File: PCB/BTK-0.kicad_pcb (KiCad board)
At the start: 4 copper layers, 167.1 x 105 mm, 110 parts, among them J1 USB_C_Receptacle_USB2.0_16P, J2 Battery, J3 Conn_01x16_Pin, J4 Conn_01x16_Socket, SW1 EN, SW10 1,2, SW11 2,2, SW12 3,2, SW13 4,2, SW14 5,2, SW15 6,2, SW16 1,3, SW17 2,3, SW18 3,3, SW19 4,3, SW2 BOOT, SW20 5,3, SW21 6,3, SW22 1,4, SW23 2,4, SW24 3,4, SW25 4,4, SW26 5,4, SW27 6,4, SW28 1,4, SW29 2,4, SW3 RotaryEncoder_Switch_MP, SW30 3,4, SW31 4,4, SW32 5,4, SW33 6,4, SW4 1,1, SW5 2,1, SW6 3,1, SW7 4,1, SW8 5,1, SW9 6,1, U1 NCP1117-3.3_SOT223, U2 NCP1117-3.3_SOT223, U3 USBLC6-2SC6, U4 ESP32-C6-MINI-1, U5 TVS1400DRV, U6 BQ24075RGT

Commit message: new switches kailh sockets
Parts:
- SW10, SW11, SW12, SW13, SW14, SW15, SW16, SW17, SW18, SW19, SW20, SW21, SW22, SW23, SW24, SW25, SW26, SW27, SW28, SW29, SW30, SW31, SW32, SW33, SW4, SW5, SW6, SW7, SW8, SW9: footprint kb_switch:SW_MX_reversible -> kb_switch:Kailh_socket_MX_reversible
- moved H4 266.2 mm to (131.5, 72.5)
- moved H3 160.4 mm to (135.3, 10.8)
- moved H1 156.3 mm to (37.0, 2.00)
- moved D33 155.2 mm to (133.6, 76.2), turned to 135 degrees
- moved D35 150.3 mm to (133.8, 20.7), turned to 180 degrees
- moved D34 150.2 mm to (133.8, 39.7)
- moved D32 144.9 mm to (113.5, 94.1), turned to 180 degrees
- moved J4 144.5 mm to (138.6, 34.3)
- moved SW10 144.5 mm to (8.84, 27.6), turned to 180 degrees
- moved SW11 144.5 mm to (27.9, 27.6), turned to 180 degrees
- moved SW12 144.5 mm to (46.9, 24.6), turned to 180 degrees
- moved SW13 144.5 mm to (66.0, 22.6), turned to 180 degrees
- moved SW14 144.5 mm to (85.0, 24.6), turned to 180 degrees
- moved SW15 144.5 mm to (104.1, 26.6), turned to 180 degrees
- moved SW16 144.5 mm to (8.84, 46.7), turned to 180 degrees
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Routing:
- net /IO1: track 233.0 -> 295.2 mm, vias 1 -> 6
- net /IO4: track 287.1 -> 339.5 mm, vias 0 -> 5
- net /IO2: track 193.0 -> 245.0 mm, vias 1 -> 6
- net /IO5: track 271.3 -> 322.5 mm, vias 0 -> 5
- net /IO0: track 252.9 -> 302.6 mm, vias 1 -> 6
- net /IO23: track 54.9 -> 16.5 mm
- net /IO18: track 185.2 -> 151.5 mm, vias 3 -> 2
- net /IO15: track 168.4 -> 138.9 mm, vias 1 -> 2
- net /IO7: track 159.2 -> 170.2 mm, vias 1 -> 6
- net Net-(D34-A): track 15.8 -> 5.08 mm, vias 0 -> 1
- net /IO14: track 150.6 -> 140.9 mm, vias 1 -> 2
- net Net-(D35-A): track 14.1 -> 5.08 mm, vias 0 -> 1
- net /IO22: track 41.6 -> 47.7 mm
- net Net-(D33-A): track 11.0 -> 5.08 mm, vias 0 -> 1
- net /IO6: track 149.4 -> 145.2 mm
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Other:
- board size 167.1 x 105 mm -> 162.1 x 105 mm

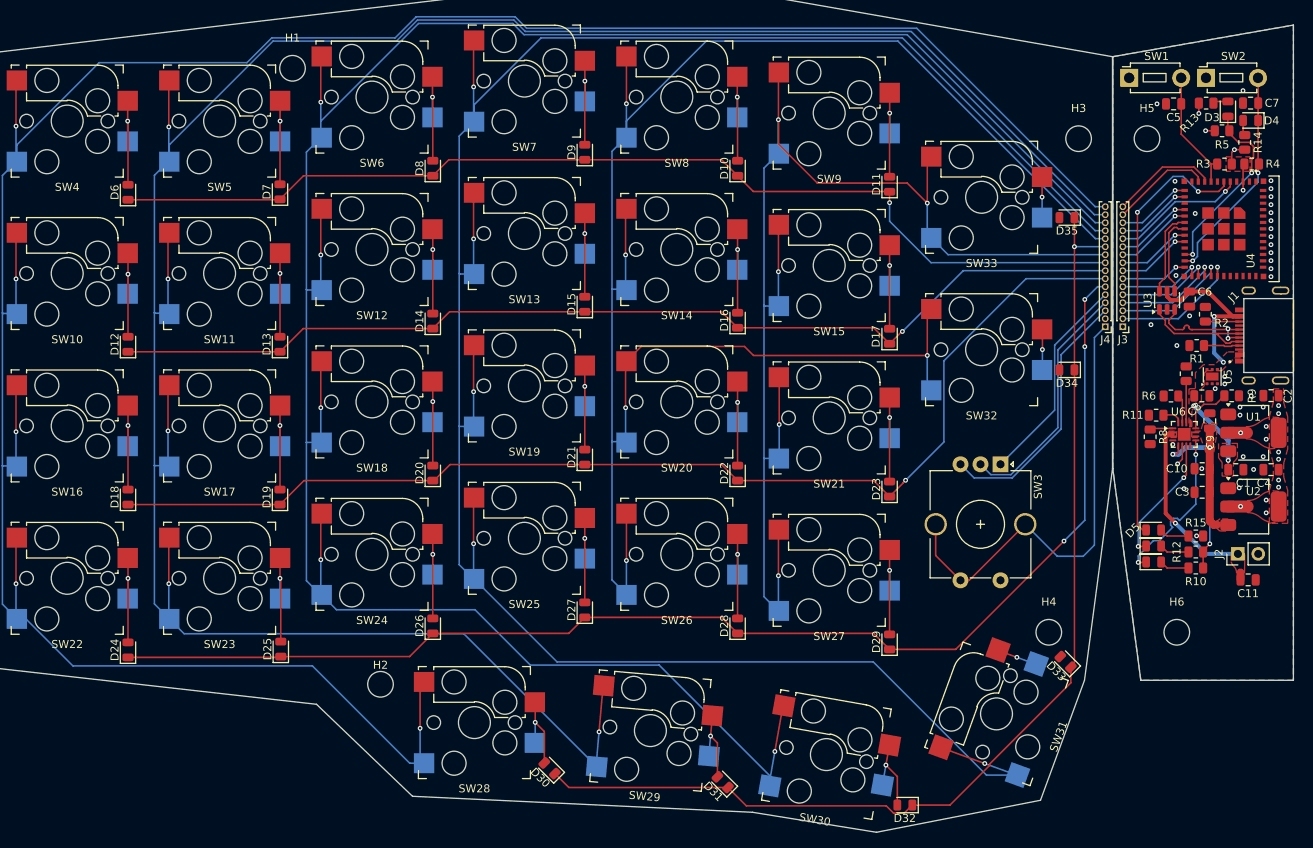
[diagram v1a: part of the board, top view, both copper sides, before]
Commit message: fixed power scheme, on/off switch to power
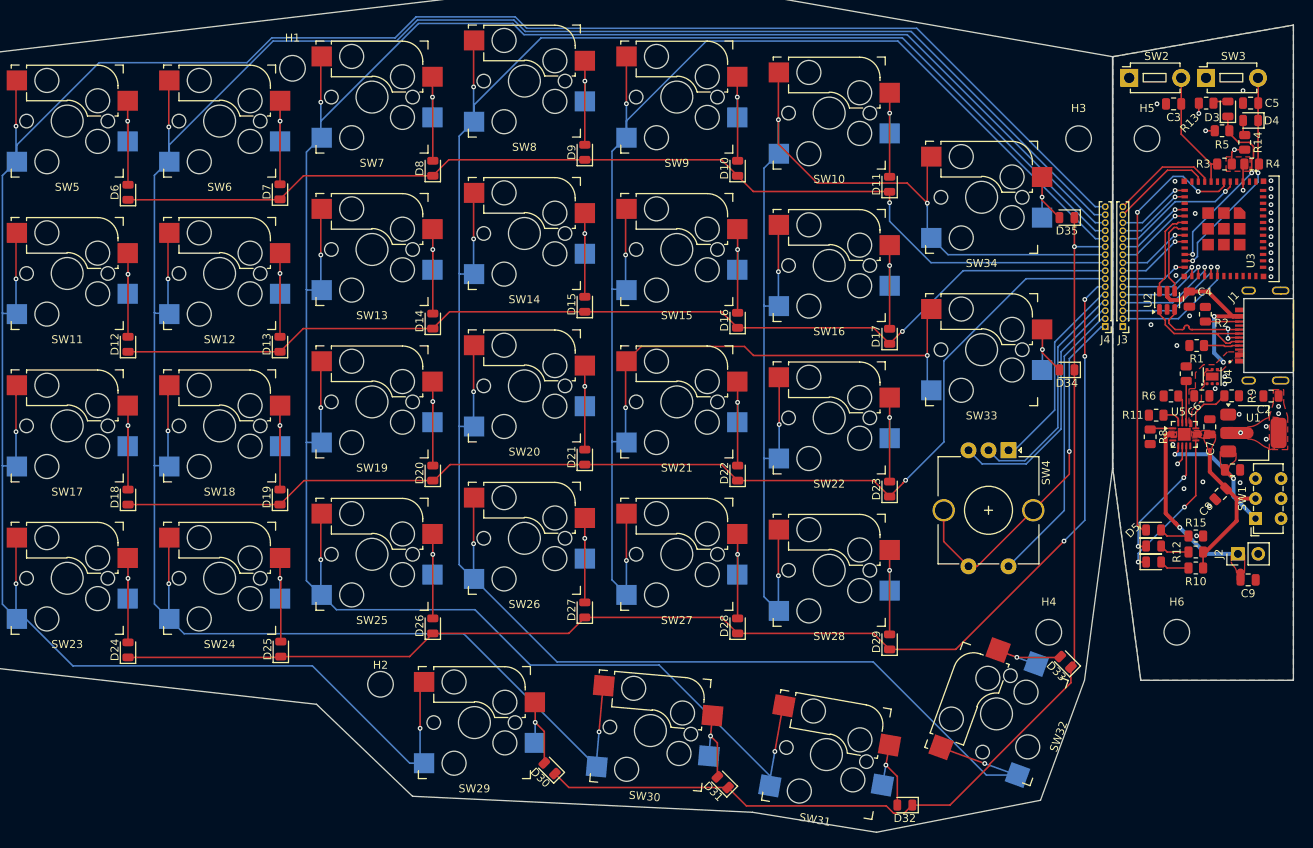
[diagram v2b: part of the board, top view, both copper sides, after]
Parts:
- removed the C1 at (154.9, 52.2)
- removed the C2 at (159.3, 42.9)
- removed the U1 at (157.1, 47.6)
- added SW1: SW_SPDT, Button_Switch_THT:SW_E-Switch_EG1271_SPDT, F.Cu at (157.4, 58.3)
- moved C2 9.20 mm to (159.3, 43.0)
- moved U1 9.20 mm to (157.1, 47.6)
- moved C1 4.71 mm to (154.5, 52.2), turned to 0 degrees
- moved C8 3.91 mm to (153.0, 55.2), turned to -135 degrees
- moved SW4 2.02 mm to (126.5, 49.8)
- moved C7 0.75 mm to (151.7, 46.8)
- renumbered C3 to C1, C4 to C2, C5 to C3, C6 to C4, C7 to C5, C8 to C6, C9 to C7, C10 to C8, C11 to C9, SW9 to SW10, SW10 to SW11, SW11 to SW12, SW12 to SW13, SW13 to SW14, SW14 to SW15, SW15 to SW16, SW16 to SW17, SW17 to SW18, SW18 to SW19, SW1 to SW2, SW19 to SW20, SW20 to SW21, SW21 to SW22, SW22 to SW23, SW23 to SW24, SW24 to SW25, SW25 to SW26, SW26 to SW27, SW27 to SW28, SW28 to SW29, SW2 to SW3, SW29 to SW30, SW30 to SW31, SW31 to SW32, SW32 to SW33, SW33 to SW34, SW3 to SW4, SW4 to SW5, SW5 to SW6, SW6 to SW7, SW7 to SW8, SW8 to SW9, U2 to U1, U3 to U2, U4 to U3, U5 to U4, U6 to U5
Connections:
- C7 pad 1: VCC -> VOUT
- C8 pad 1: VCC -> VOUT
- R10 pad 1: VCC -> VOUT
- R12 pad 2: VCC -> VOUT
- U5 pad 10: VCC -> VOUT
- U5 pad 11: VCC -> VOUT
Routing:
- net /IO23: track 16.5 -> 52.8 mm
- net VOUT: track 0.00 -> 21.7 mm
- net VCC: track 35.8 -> 18.3 mm, vias 3 -> 2
- net GND: track 60.5 -> 48.8 mm, vias 36 -> 32
- net VBUS: track 30.1 -> 21.0 mm, vias 4 -> 2
- net Net-(D33-A): track 5.08 -> 10.6 mm
- net Net-(D35-A): track 5.08 -> 8.54 mm
- net Net-(D34-A): track 5.08 -> 8.50 mm
- net +3V3: track 14.8 -> 12.5 mm, vias 17 -> 10
- net Net-(D2-K): track 20.7 -> 19.2 mm
- net /IO21: track 44.2 -> 42.7 mm
- net /IO22: track 47.7 -> 46.2 mm
- net /IO20: track 38.7 -> 37.2 mm
- added copper zone on F.Cu, net VOUT

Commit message: exported cad
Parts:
- moved D10 141.5 mm to (-48.9, 13.9)
- moved D11 141.5 mm to (-29.9, 15.9)
- moved D12 141.5 mm to (-125.1, 36.0)
- moved D13 141.5 mm to (-106.1, 36.0)
- moved D14 141.5 mm to (-87.0, 33.0)
- moved D15 141.5 mm to (-68.0, 30.9)
- moved D16 141.5 mm to (-48.9, 33.0)
- moved D17 141.5 mm to (-29.9, 35.0)
- moved D18 141.5 mm to (-125.1, 55.0)
- moved D19 141.5 mm to (-106.1, 55.0)
- moved D20 141.5 mm to (-87.0, 52.0)
- moved D21 141.5 mm to (-68.0, 50.0)
- moved D22 141.5 mm to (-48.9, 52.0)
- moved D23 141.5 mm to (-29.9, 54.0)
- moved D24 141.5 mm to (-125.1, 74.2)
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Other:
- board size 162.1 x 105 mm -> 164.1 x 105 mm

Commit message: alignment
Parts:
- moved J4 4.17 mm to (-7.00, 33.0)
- moved H3 3.77 mm to (-10.0, 10.0)
- moved D33 3.00 mm to (-10.9, 75.7)
- moved D10 3.00 mm to (-51.9, 13.9)
- moved D12 3.00 mm to (-128.1, 36.0)
- moved D13 3.00 mm to (-109.1, 36.0)
- moved D14 3.00 mm to (-90.0, 33.0)
- moved D15 3.00 mm to (-71.0, 30.9)
- moved D16 3.00 mm to (-51.9, 33.0)
- moved D18 3.00 mm to (-128.1, 55.0)
- moved D19 3.00 mm to (-109.1, 55.0)
- moved D20 3.00 mm to (-90.0, 52.0)
- moved D21 3.00 mm to (-71.0, 50.0)
- moved D22 3.00 mm to (-51.9, 52.0)
- moved D24 3.00 mm to (-128.1, 74.2)
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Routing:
- net /IO3: track 54.7 -> 15.6 mm
- net /IO1: track 295.2 -> 285.5 mm
- net /IO5: track 322.5 -> 320.0 mm
- net /IO2: track 245.0 -> 242.6 mm
- net /IO4: track 339.5 -> 337.0 mm
- net /IO0: track 302.6 -> 300.2 mm
- net /IO6: track 145.2 -> 143.1 mm
- net /IO14: track 140.9 -> 138.8 mm
- net /IO15: track 138.9 -> 137.1 mm
- net /IO18: track 151.5 -> 149.9 mm
- net /IO7: track 170.2 -> 168.7 mm
- net /IO23: track 52.8 -> 52.1 mm
- net /IO21: track 42.7 -> 42.1 mm
- net /IO22: track 46.2 -> 45.6 mm
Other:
- board size 164.1 x 105 mm -> 167.1 x 105 mm

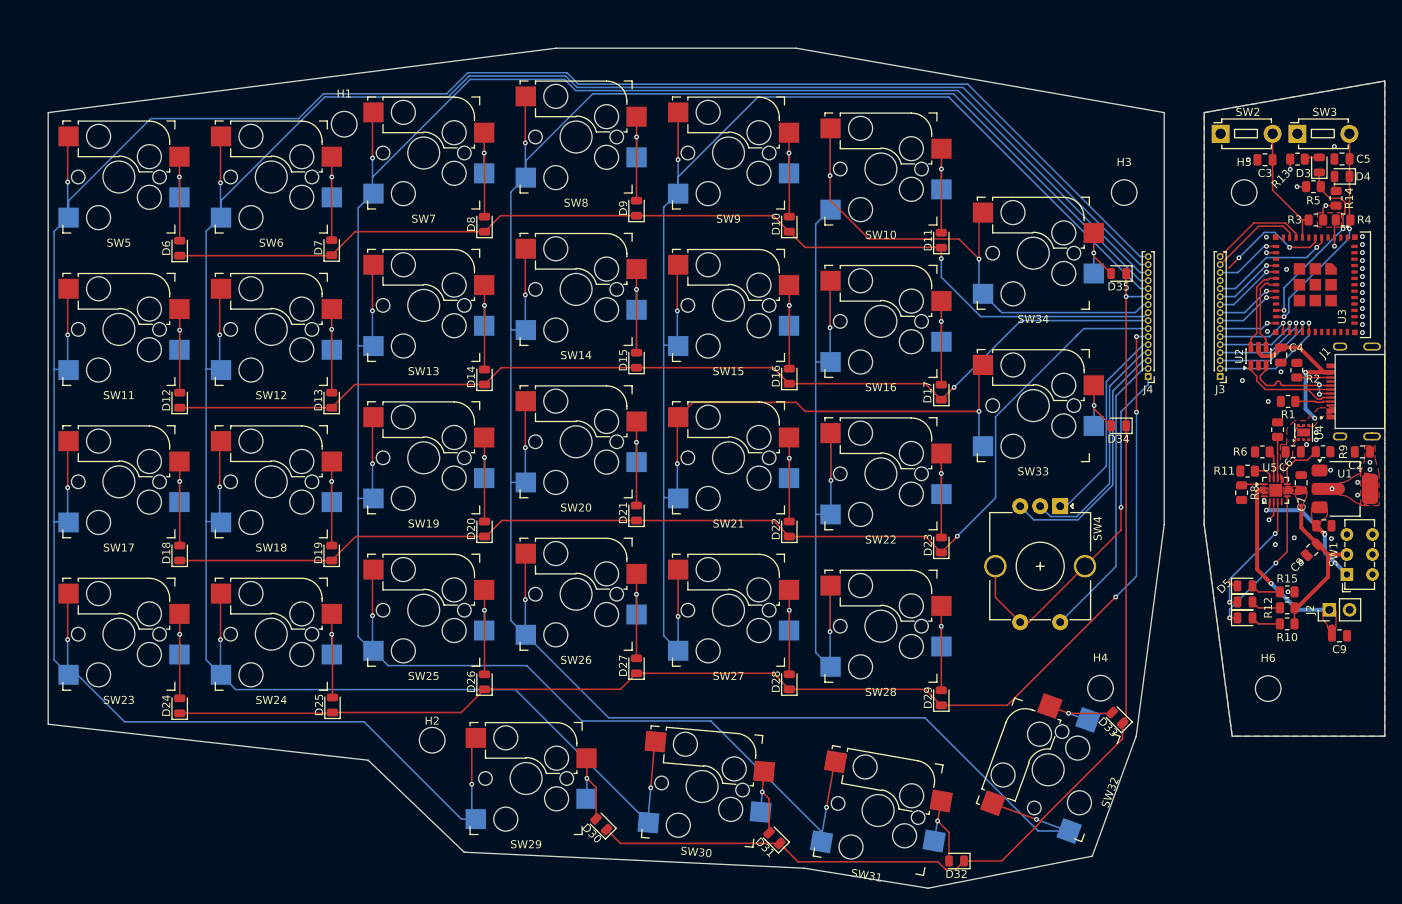
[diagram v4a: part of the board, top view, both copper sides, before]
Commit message: fixed rollback, alignment and powerswitch redone
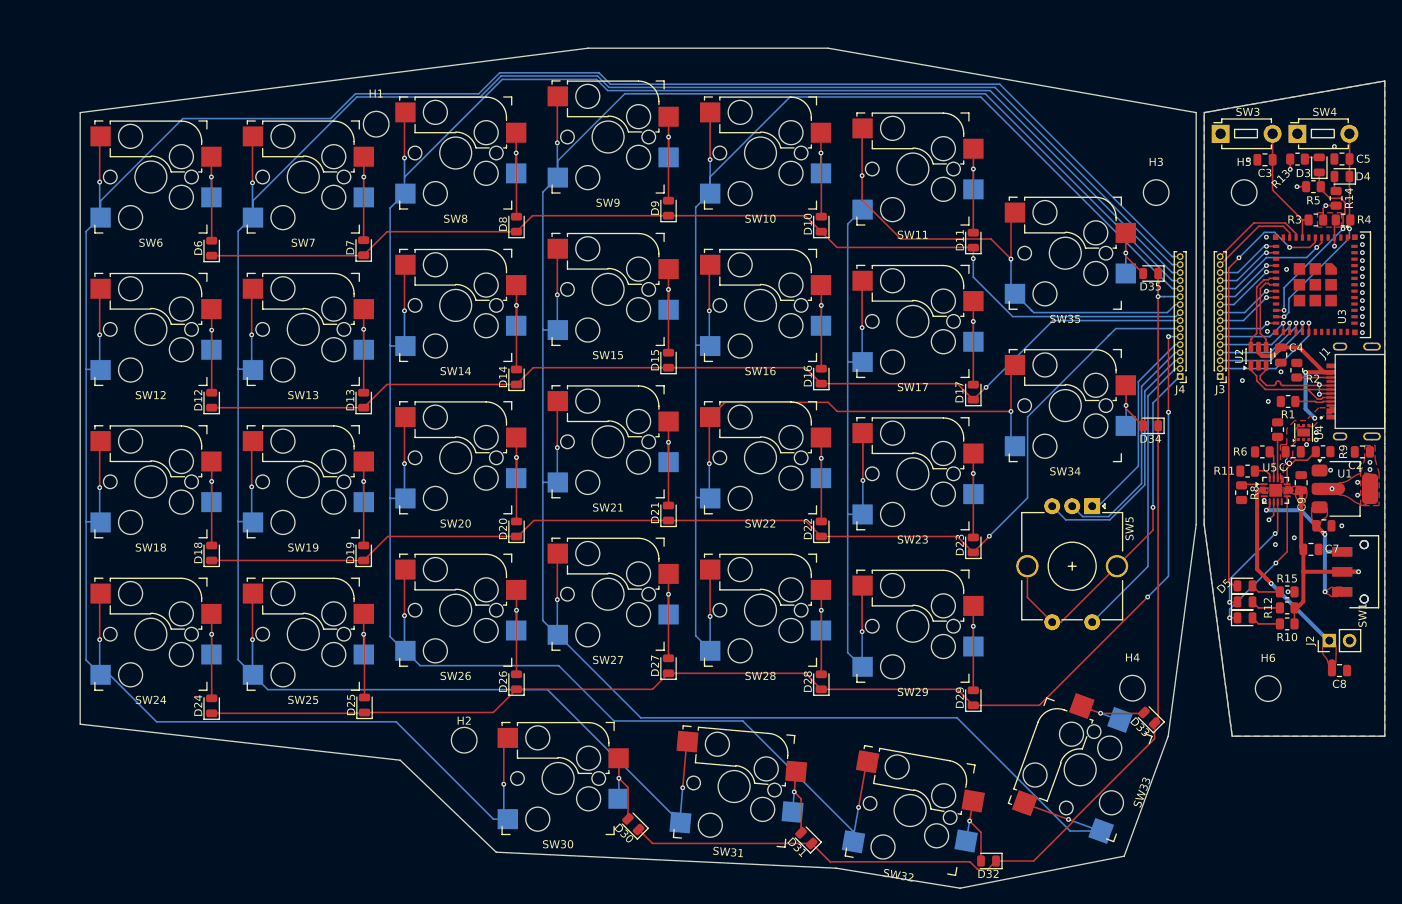
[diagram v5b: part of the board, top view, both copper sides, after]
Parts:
- added SW2: SW_SPDT, JS102011SAQN:SW_JS102011SAQN, B.Cu at (20.0, 57.4)
- C7: renamed from C8; value 4.7u -> 10u
- SW1: footprint Button_Switch_THT:SW_E-Switch_EG1271_SPDT -> JS102011SAQN:SW_JS102011SAQN
- moved C8 4.35 mm to (16.9, 69.8)
- moved D33 4.00 mm to (-6.86, 75.7)
- moved D10 4.00 mm to (-47.9, 13.9)
- moved D12 4.00 mm to (-124.1, 36.0)
- moved D13 4.00 mm to (-105.1, 36.0)
- moved D14 4.00 mm to (-86.0, 33.0)
- moved D15 4.00 mm to (-67.0, 30.9)
- moved D16 4.00 mm to (-47.9, 33.0)
- moved D18 4.00 mm to (-124.1, 55.0)
- moved D19 4.00 mm to (-105.1, 55.0)
- moved D20 4.00 mm to (-86.0, 52.0)
- moved D21 4.00 mm to (-67.0, 50.0)
- moved D22 4.00 mm to (-47.9, 52.0)
- moved D24 4.00 mm to (-124.1, 74.2)
- moved D25 4.00 mm to (-105.0, 74.0)
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- renumbered C9 to C8, C7 to C9, SW9 to SW10, SW10 to SW11, SW11 to SW12, SW12 to SW13, SW13 to SW14, SW14 to SW15, SW15 to SW16, SW16 to SW17, SW17 to SW18, SW18 to SW19, SW19 to SW20, SW20 to SW21, SW21 to SW22, SW22 to SW23, SW23 to SW24, SW24 to SW25, SW25 to SW26, SW26 to SW27, SW27 to SW28, SW28 to SW29, SW2 to SW3, SW29 to SW30, SW30 to SW31, SW31 to SW32, SW32 to SW33, SW33 to SW34, SW34 to SW35, SW3 to SW4, SW4 to SW5, SW5 to SW6, SW6 to SW7, SW7 to SW8, SW8 to SW9
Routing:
- net /IO3: track 15.6 -> 54.7 mm
- net /IO1: track 285.5 -> 292.7 mm
- net VOUT: track 21.7 -> 27.7 mm, vias 0 -> 1
- net VCC: track 18.3 -> 21.6 mm, vias 2 -> 3
- net VBAT: track 23.7 -> 24.9 mm
- net GND: vias 32 -> 31
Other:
- board size 167.1 x 105 mm -> 163.1 x 105 mm

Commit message: left board, step files, and production files done
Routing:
- net GND: vias 31 -> 267

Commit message: fixing rotary encoder pin
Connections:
- J3 pad 4: /IO21 -> GND
- J4 pad 4: /IO21 -> GND
- SW5 pad C: /IO21 -> GND
- U3 pad 27: /IO21 -> unconnected-(U3-IO21-Pad27)
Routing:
- net GND: track 48.8 -> 2.51 mm
- net /IO21: track 42.1 -> 0.00 mm, vias 1 -> 0
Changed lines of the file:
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@@
 		(capping no)
 		(filling no)
-		(zone_defaults)
 		(pcbplotparams
 			(layerselection 0x00000000_00000000_55555555_5755f5ff)
@@
 			(layers "*.Cu" "*.Mask")
 			(remove_unused_layers no)
-			(net "/IO21")
+			(net "GND")
 			(pinfunction "C_C")
 			(pintype "passive")
@@
 			(size 0.8 0.4)
 			(layers "F.Cu" "F.Mask" "F.Paste")
-			(net "/IO21")
+			(net "unconnected-(U3-IO21-Pad27)")
 			(pinfunction "IO21_27")
-			(pintype "bidirectional")
+			(pintype "bidirectional+no_connect")
 			(solder_mask_margin 0.102)
 		)
@@
 			(layer "F.Fab")
 		)
+		(fp_poly
+			(pts
+				(xy -14.287502 -9.524997) (xy 14.287498 -9.524997) (xy 14.287498 9.525003) (xy -14.287502 9.525003)
+			)
+			(stroke
+				(width 0.1)
+				(type default)
+			)
+			(fill no)
+			(layer "F.Fab")
+		)
 		(fp_text user "${REFERENCE}"
 			(at 0 -8.255 70)
@@
 			(layers "*.Cu" "*.Mask")
 			(remove_unused_layers no)
-			(net "/IO21")
+			(net "GND")
 			(pinfunction "Pin_4_4")
 			(pintype "passive")
@@
 			(layers "*.Cu" "*.Mask")
 			(remove_unused_layers no)
-			(net "/IO21")
+			(net "GND")
 			(pinfunction "Pin_4_4")
 			(pintype "passive")
@@
 	)
 	(segment
-		(start -19 63.7)
-		(end -22.1 60.6)
-		(width 0.2)
-		(layer "F.Cu")
-		(net "GND")
-	)
-	(segment
 		(start 8.685 48.651666)
 		(end 8.685 50.315)
@@
 	)
 	(segment
-		(start -6.4 49.35)
-		(end -6.4 52.2)
-		(width 0.2)
-		(layer "F.Cu")
-		(net "GND")
-	)
-	(segment
-		(start -22.1 60.6)
-		(end -22.1 56.7)
-		(width 0.2)
-		(layer "F.Cu")
-		(net "GND")
-	)
-	(segment
 		(start 17.289166 42.389166)
 		(end 17.3 42.4)
@@
 		(net "GND")
 	)
-	(segment
-		(start -6.4 52.2)
-		(end -10.9 56.7)
-		(width 0.2)
-		(layer "F.Cu")
-		(net "GND")
-	)
-	(segment
-		(start -17.9 63.7)
-		(end -19 63.7)
-		(width 0.2)
-		(layer "F.Cu")
-		(net "GND")
-	)
-	(segment
-		(start -10.9 56.7)
-		(end -17.9 63.7)
-		(width 0.2)
-		(layer "F.Cu")
-		(net "GND")
-	)
 	(via
 		(at -101 52)
@@
 	)
 	(segment
-		(start -3 33)
-		(end -3.1 33)
-		(width 0.2)
-		(layer "B.Cu")
-		(net "GND")
-	)
-	(segment
-		(start -6.4 36.3)
-		(end -6.4 49.35)
-		(width 0.2)
-		(layer "B.Cu")
-		(net "GND")
-	)
-	(segment
-		(start -3.1 33)
-		(end -6.4 36.3)
-		(width 0.2)
-		(layer "B.Cu")
-		(net "GND")
-	)
-	(segment
 		(start -61.8625 24.78)
 		(end -61.8625 18.99)
@@
 	)
 	(segment
-		(start 11.485 26.3)
-		(end 11.485 27.42)
-		(width 0.2)
-		(layer "F.Cu")
-		(net "/IO21")
-	)
-	(via
-		(at 11.485 26.3)
-		(size 0.6)
-		(drill 0.3)
-		(layers "F.Cu" "B.Cu")
-		(net "/IO21")
-	)
-	(segment
-		(start -7.8275 46.3775)
-		(end -11.95 50.5)
-		(width 0.2)
-		(layer "B.Cu")
-		(net "/IO21")
-	)
-	(segment
-		(start 11.485 26.756764)
-		(end 11.485 26.3)
-		(width 0.2)
-		(layer "B.Cu")
-		(net "/IO21")
-	)
-	(segment
-		(start -7.8275 34.226465)
-		(end -7.8275 46.3775)
-		(width 0.2)
-		(layer "B.Cu")
-		(net "/IO21")
-	)
-	(segment
-		(start -2.999996 30.000001)
-		(end -3.601036 30.000001)
-		(width 0.2)
-		(layer "B.Cu")
-		(net "/IO21")
-	)
-	(segment
-		(start -11.95 50.5)
-		(end -15.2 50.5)
-		(width 0.2)
-		(layer "B.Cu")
-		(net "/IO21")
-	)
-	(segment
-		(start 8.241763 30.000001)
-		(end 2.000004 30.000001)
-		(width 0.2)
-		(layer "B.Cu")
-		(net "/IO21")
-	)
-	(segment
-		(start 11.485 26.756764)
-		(end 8.241763 30.000001)
-		(width 0.2)
-		(layer "B.Cu")
-		(net "/IO21")
-	)
-	(segment
-		(start -15.2 50.5)
-		(end -16.5 49.2)
-		(width 0.2)
-		(layer "B.Cu")
-		(net "/IO21")
-	)
-	(segment
-		(start -3.601036 30.000001)
-		(end -7.8275 34.226465)
-		(width 0.2)
-		(layer "B.Cu")
-		(net "/IO21")
-	)
-	(segment
